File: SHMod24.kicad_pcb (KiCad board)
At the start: 2 copper layers, 49.5 x 49.5 mm, 47 parts, among them IC1 ArduinoProMini, J1 Conn_02x14_Odd_Even, J2 Conn_01x01, J3 Conn_01x01, J4 RESET, J5 12V, J6 GND, Q1 FS8205A, U1 ESP-12, U2 NRF24L01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

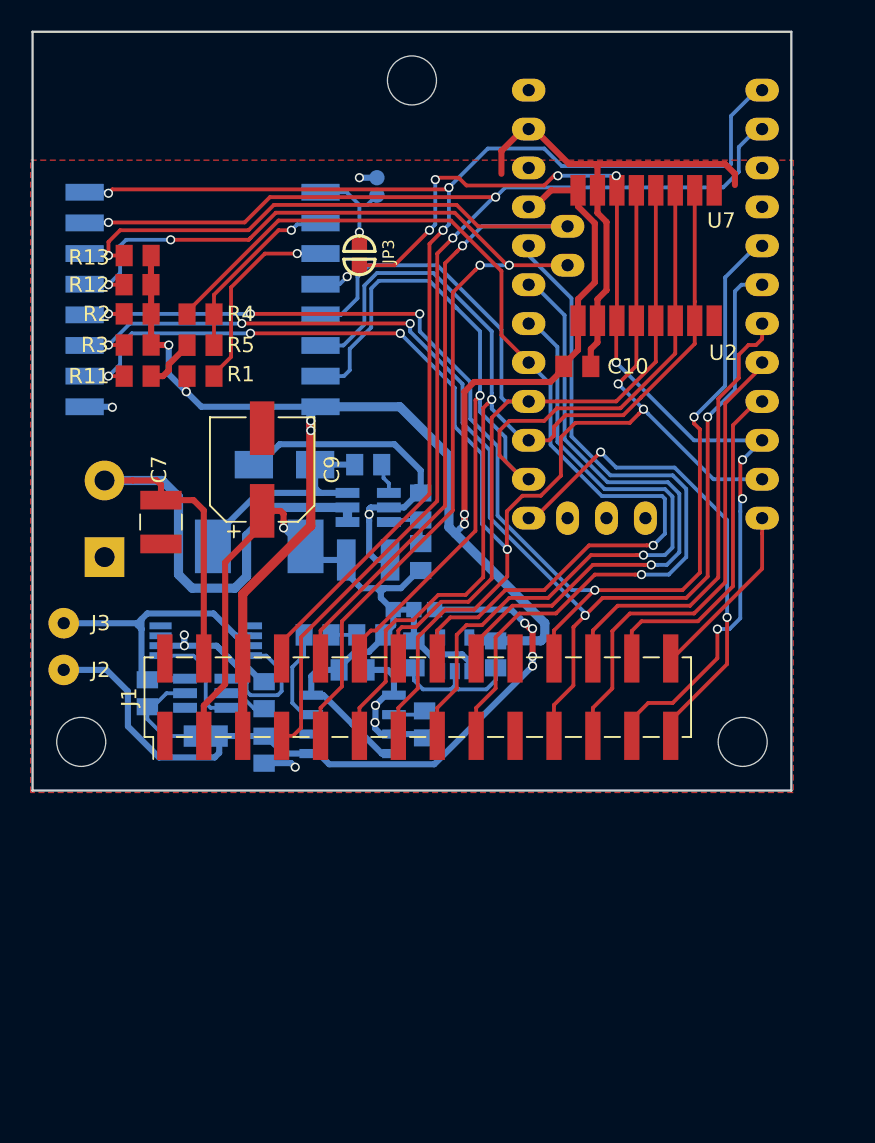
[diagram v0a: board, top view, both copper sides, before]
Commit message: add RS485 and MOSFETs
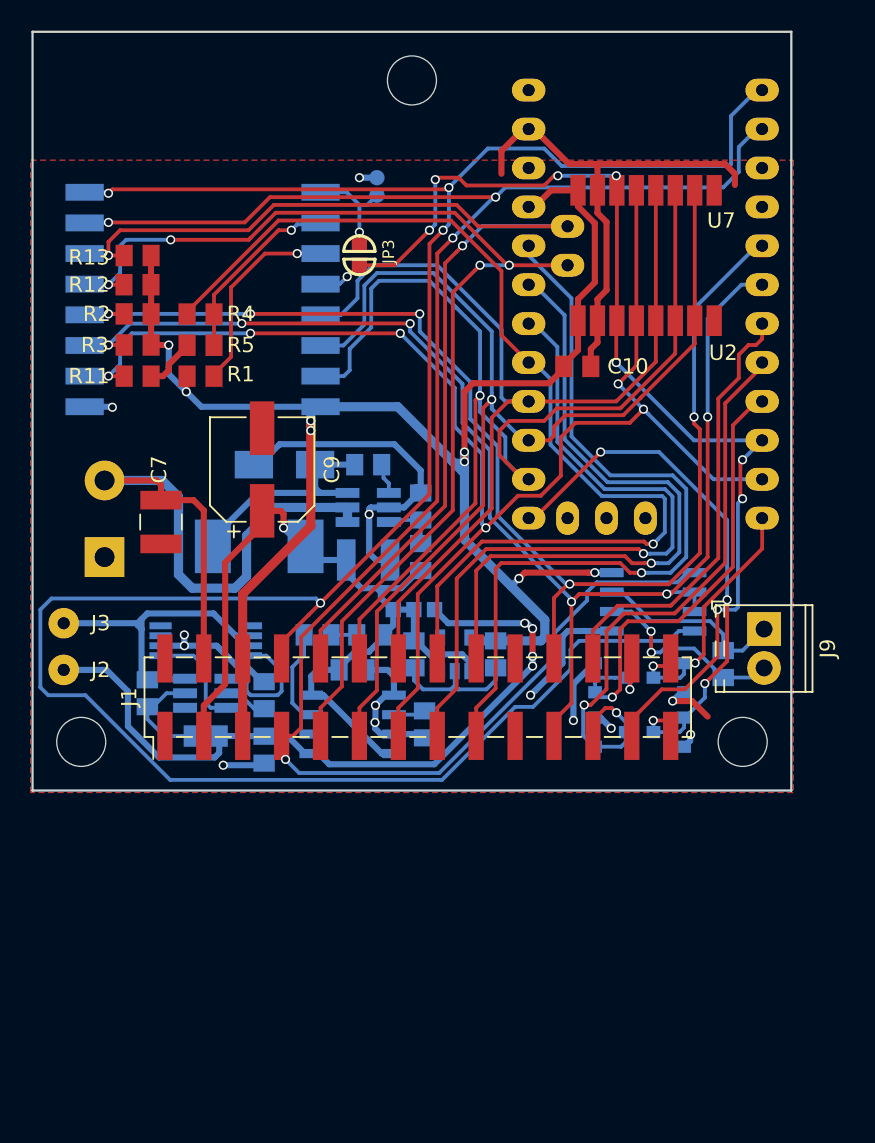
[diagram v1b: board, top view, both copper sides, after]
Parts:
- added J9: Screw_Terminal_01x02, LeoDJ-kicad:TerminalBlock_Phoenix_MPT-0,5-2-2.54_1x02_P2.54mm_Horizontal_fixed, F.Cu at (98.6, 101.2)
- added Q2: AO3400A, Package_TO_SOT_SMD:SOT-23, B.Cu at (88.5, 104.4)
- added Q3: AO3400A, Package_TO_SOT_SMD:SOT-23, B.Cu at (92.3, 104.4)
- added Q4: AO3400A, Package_TO_SOT_SMD:SOT-23, B.Cu at (88.5, 108.0)
- added Q5: AO3400A, Package_TO_SOT_SMD:SOT-23, B.Cu at (92.3, 108.0)
- added R15: 120, Resistor_SMD:R_0805_2012Metric, B.Cu at (95.9, 103.5)
- added U8: MAX3485, Package_SO:SOIC-8_3.9x4.9mm_P1.27mm, B.Cu at (91.3, 99.4)
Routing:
- net TX: track 84.5 -> 158.3 mm, vias 3 -> 4
- net RX: track 89.2 -> 124.6 mm, vias 3 -> 4
- net GND: track 81.8 -> 100.9 mm, vias 8 -> 13
- net Net-(J9-Pad2): track 0.00 -> 13.0 mm, vias 0 -> 2
- net Net-(J9-Pad1): track 0.00 -> 12.7 mm
- net P06: track 22.7 -> 32.5 mm, vias 0 -> 2
- net P05: track 31.4 -> 39.7 mm, vias 0 -> 2
- net P09: track 11.7 -> 19.9 mm, vias 0 -> 2
- net P10: track 32.5 -> 36.5 mm, vias 2 -> 4
- net +3V3: track 108.1 -> 111.4 mm, vias 6 -> 8
- net A3: track 48.5 -> 51.7 mm
- net A2: track 40.8 -> 43.9 mm
- net CS: track 96.9 -> 94.0 mm
- net A1: track 44.6 -> 47.0 mm
- net GPIO2: track 85.1 -> 87.2 mm, vias 5 -> 6
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
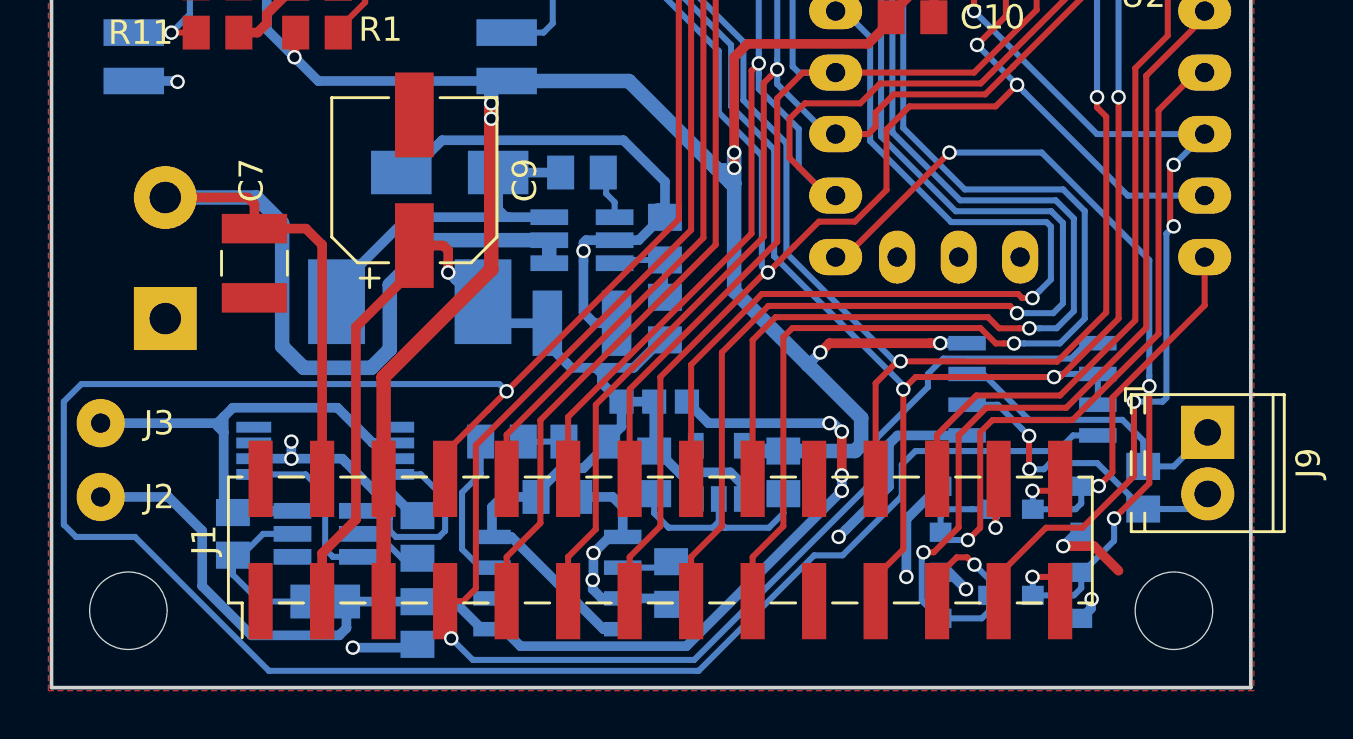
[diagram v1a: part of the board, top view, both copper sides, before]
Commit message: add MOSFET pulldowns
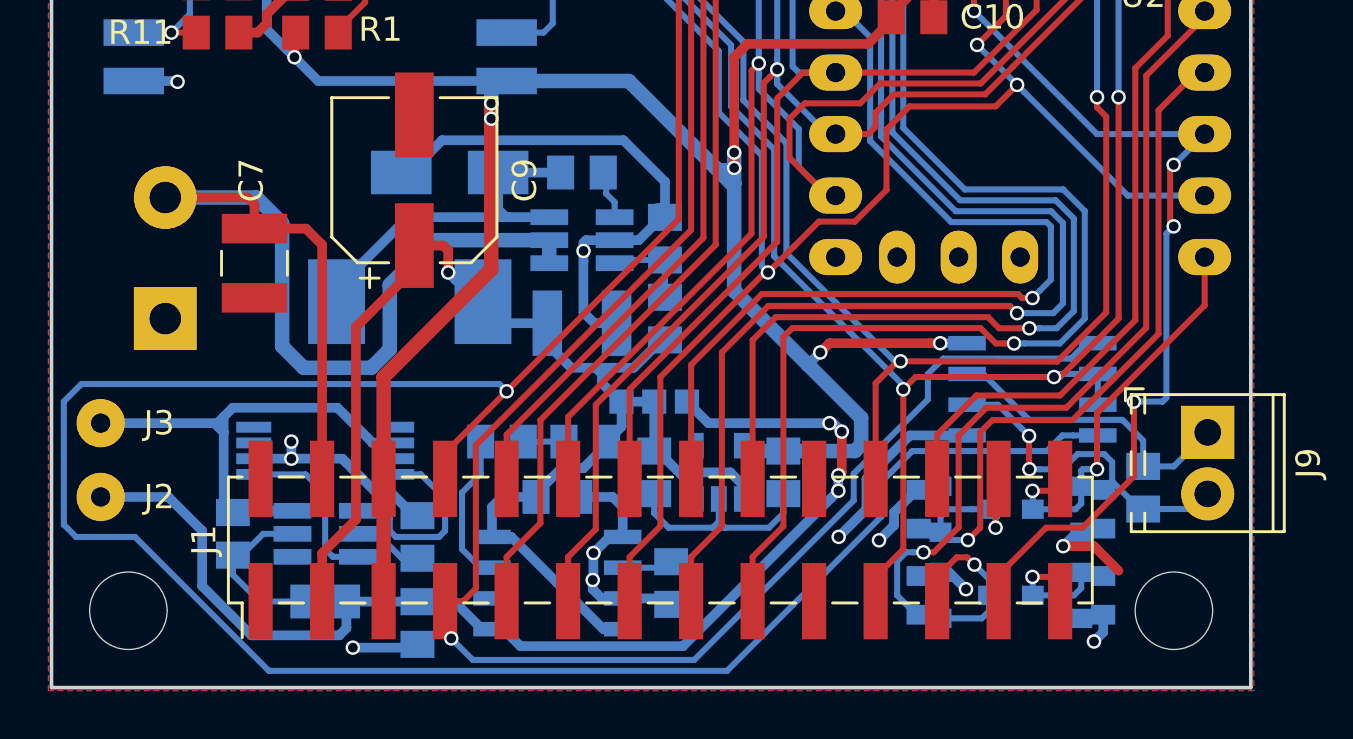
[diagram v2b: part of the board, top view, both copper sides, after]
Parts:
- added R16: 10k, Resistor_SMD:R_0603_1608Metric, B.Cu at (86.6, 104.4)
- added R17: 10k, Resistor_SMD:R_0603_1608Metric, B.Cu at (94.2, 104.4)
- added R18: 10k, Resistor_SMD:R_0603_1608Metric, B.Cu at (86.6, 108.0)
- added R19: 10k, Resistor_SMD:R_0603_1608Metric, B.Cu at (94.2, 108.0)
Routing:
- net P10: track 36.5 -> 6.82 mm, vias 4 -> 1
- net GND: track 100.9 -> 103.2 mm
- net P05: track 39.7 -> 41.6 mm
- net P06: track 32.5 -> 33.5 mm
- net P09: track 19.9 -> 20.8 mm
- net Net-(J9-Pad2): track 13.0 -> 13.8 mm

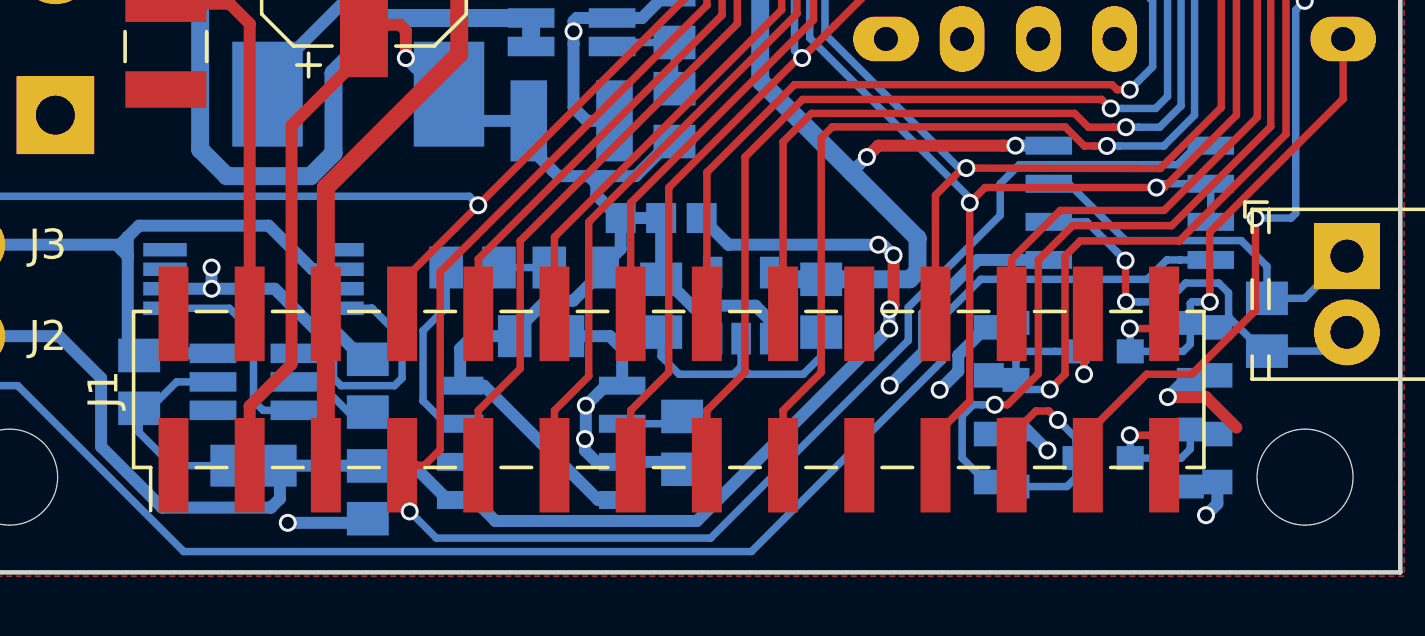
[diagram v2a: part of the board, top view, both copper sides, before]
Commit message: add fifth MOSFET
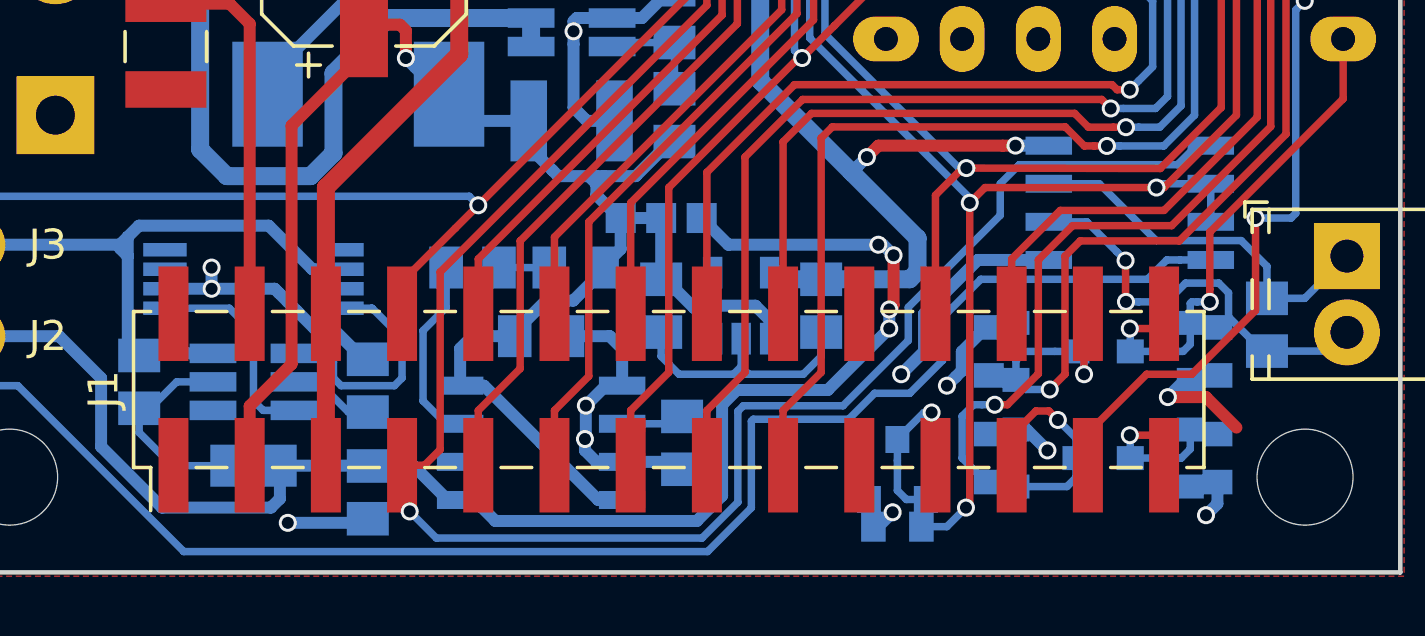
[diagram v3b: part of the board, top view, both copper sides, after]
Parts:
- added Q6: AO3400A, Package_TO_SOT_SMD:SOT-23, B.Cu at (83.6, 108.3)
- added R20: 10k, Resistor_SMD:R_0603_1608Metric, B.Cu at (83.6, 110.2)
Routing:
- net GPIO2: track 87.2 -> 98.0 mm, vias 6 -> 8
- net RX: track 124.6 -> 126.4 mm
- net +BATT: track 48.2 -> 50.0 mm
- net TX: track 158.4 -> 160.1 mm
- net GND: track 103.2 -> 104.2 mm, vias 13 -> 14

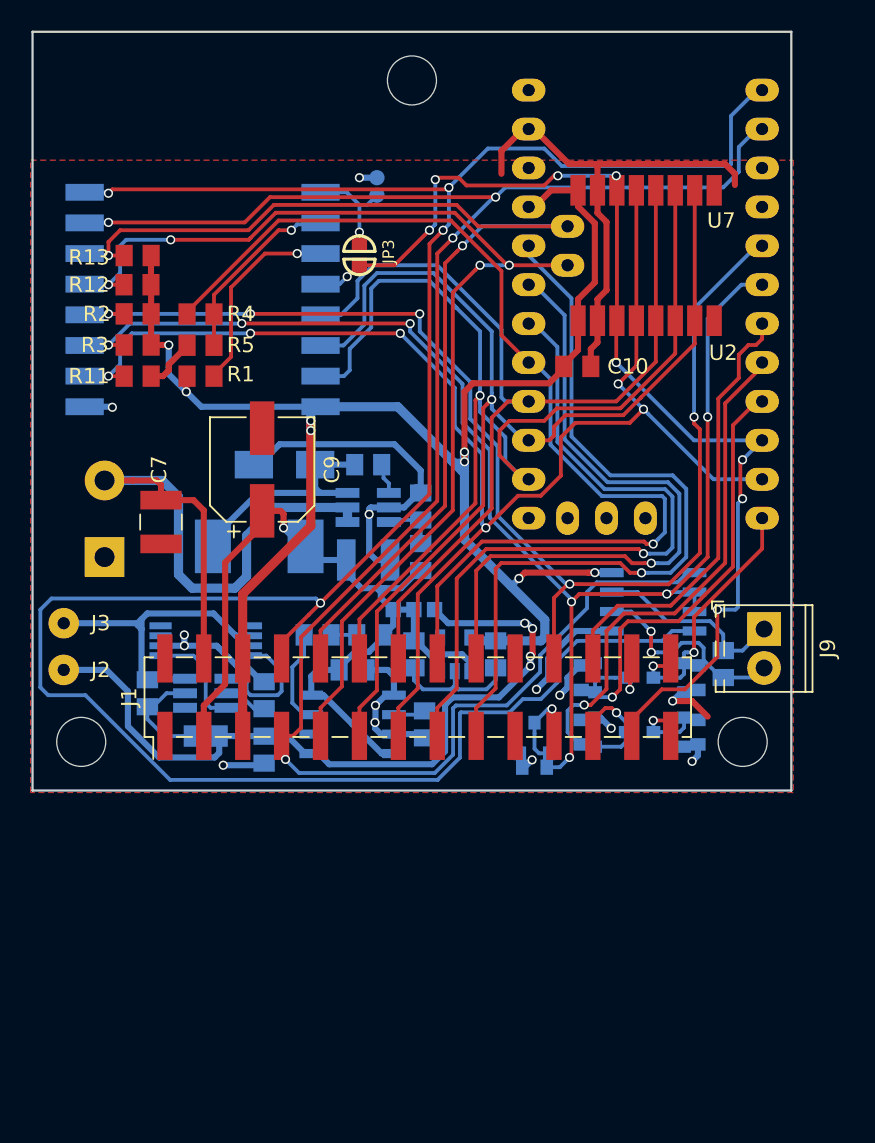
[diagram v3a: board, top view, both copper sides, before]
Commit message: add high voltage sense input
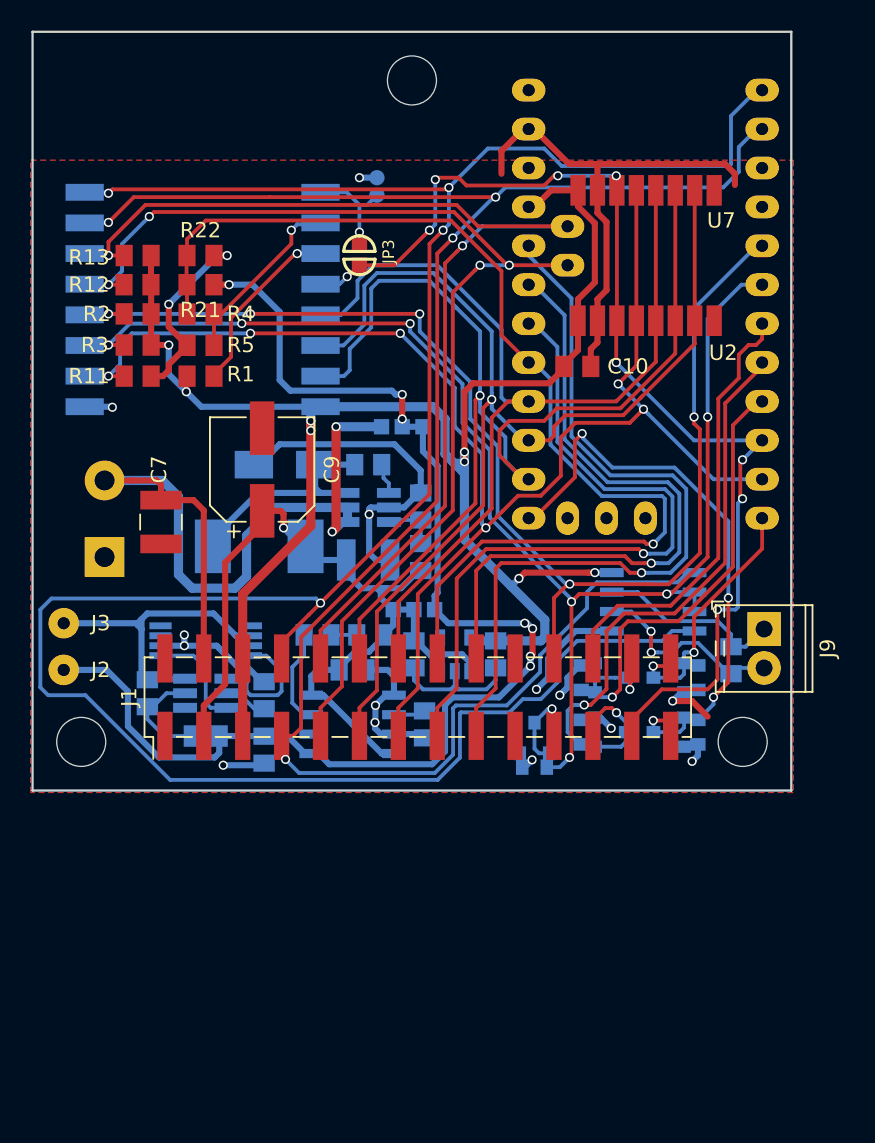
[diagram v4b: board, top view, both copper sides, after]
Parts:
- added JP2: VoltSense, LeoDJ-kicad:SOLDER-JUMPER_2-WAY, B.Cu at (74.9, 88.0)
- added R21: 47k/220k, Resistor_SMD:R_0805_2012Metric, F.Cu at (61.8, 78.7)
- added R22: 22k, Resistor_SMD:R_0805_2012Metric, F.Cu at (61.8, 76.8)
- moved R15 0.57 mm to (96.4, 103.3)
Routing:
- net +BATT: track 50.0 -> 83.7 mm, vias 4 -> 7
- net P10: track 6.82 -> 39.5 mm, vias 1 -> 4
- net VCC: track 44.0 -> 55.2 mm, vias 0 -> 2
- net GND: track 104.2 -> 113.4 mm, vias 14 -> 16
- net A0: track 70.7 -> 73.7 mm
- net +3V3: track 111.4 -> 112.8 mm
- net Net-(R1-Pad1): track 12.3 -> 11.1 mm
- net GPIO16: track 73.5 -> 74.4 mm

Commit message: begin switching regulator improvement
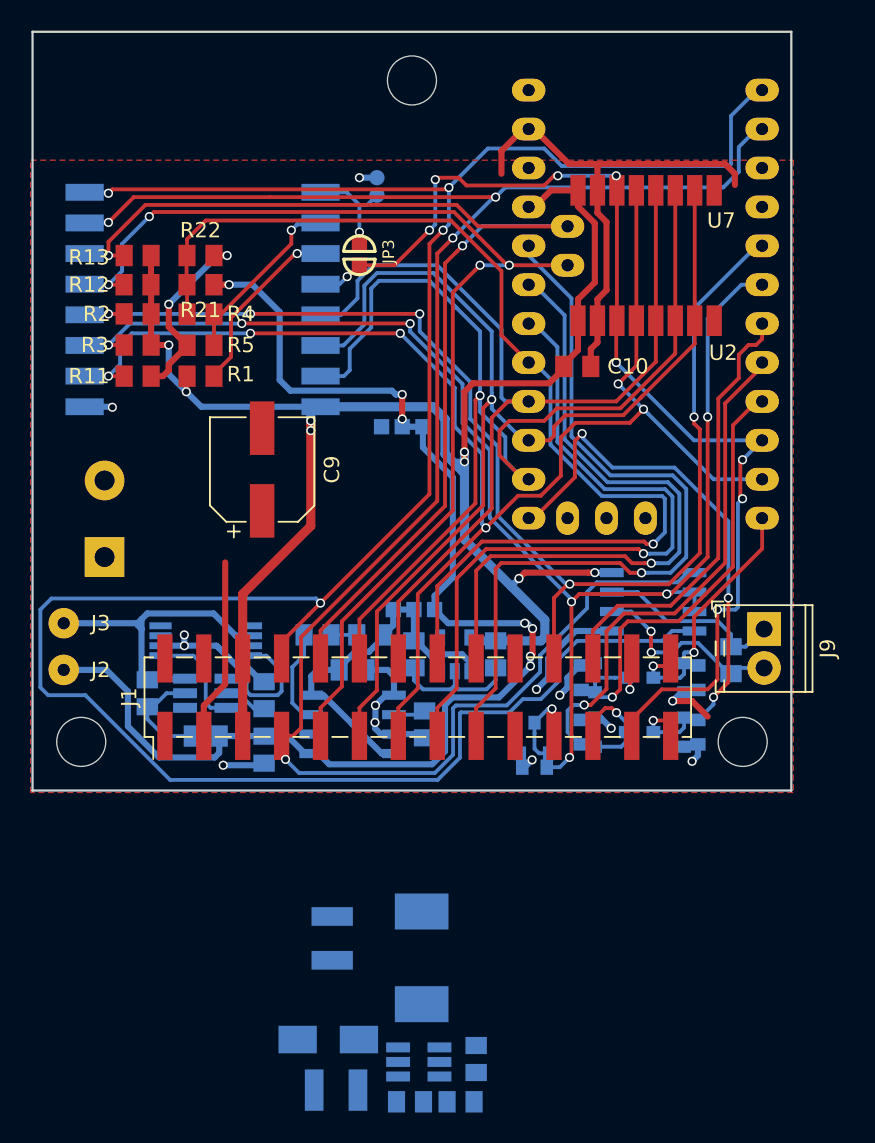
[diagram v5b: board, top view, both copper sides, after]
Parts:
- C7: moved to B.Cu
- moved C6 39.4 mm to (79.8, 129.3), turned to 90 degrees
- moved R10 38.9 mm to (75.4, 132.1), turned to 180 degrees
- moved C7 38.8 mm to (70.6, 131.3), turned to 180 degrees
- moved D1 37.6 mm to (70.1, 128.0)
- moved U6 36.3 mm to (76.0, 129.5)
- moved R9 35.7 mm to (78.7, 132.1), turned to 180 degrees
- moved L1 28.9 mm to (76.2, 122.7), turned to 90 degrees
- moved C8 24.8 mm to (70.4, 121.4), turned to 270 degrees
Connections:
- U6 pad 4: VCC -> Net-(U6-Pad4)
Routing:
- net VCC: track 55.2 -> 0.00 mm, vias 2 -> 0
- net GND: track 113.4 -> 91.4 mm, vias 16 -> 15
- net +5V: track 57.3 -> 38.1 mm, vias 1 -> 0
- net /SW: track 16.9 -> 0.00 mm
- net Net-(R10-Pad1): track 3.41 -> 0.00 mm
- net Net-(C6-Pad1): track 1.99 -> 0.00 mm
- net +BATT: track 83.7 -> 84.6 mm
